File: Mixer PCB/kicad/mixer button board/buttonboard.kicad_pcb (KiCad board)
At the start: 2 copper layers, 161 x 57 mm, 58 parts, among them J1 Conn_01x02, J2 Conn_02x13_Odd_Even, sw1 cherry_sk6812, sw10 cherry_sk6812, sw11 cherry_sk6812, sw12 cherry_sk6812, sw13 cherry_sk6812, sw14 cherry_sk6812, sw15 cherry_sk6812, sw16 cherry_sk6812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

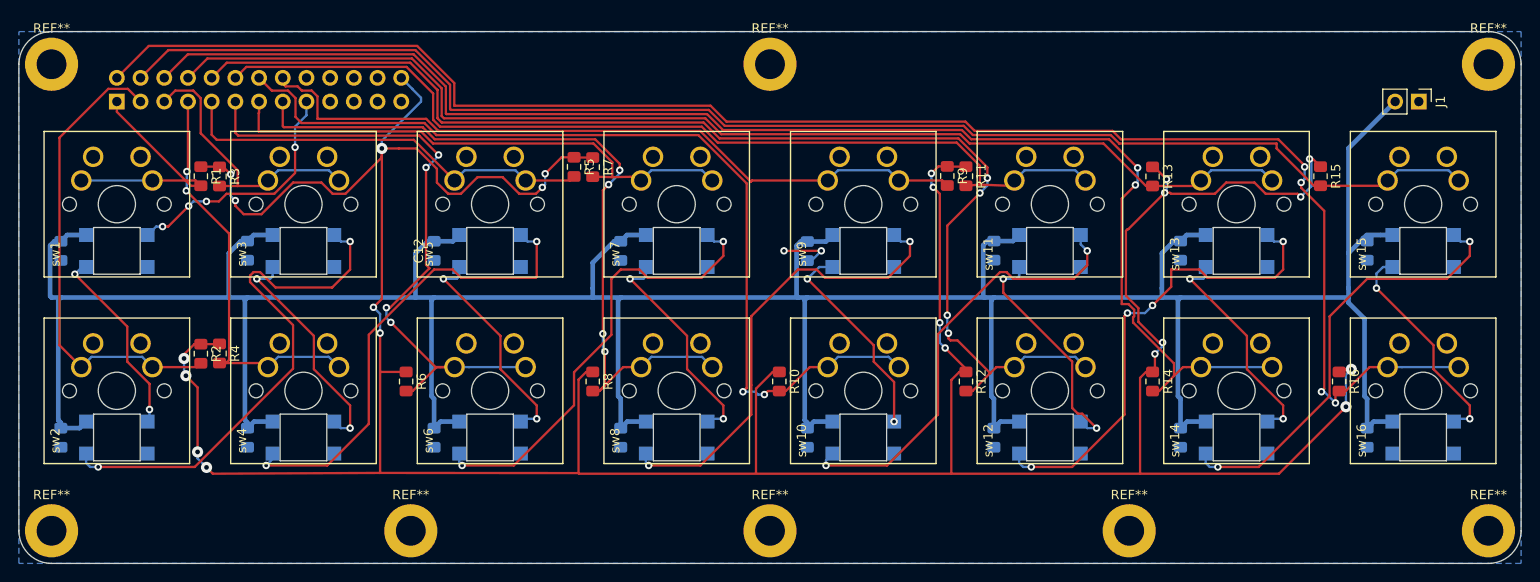
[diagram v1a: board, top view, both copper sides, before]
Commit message: Updated Button board to I2C
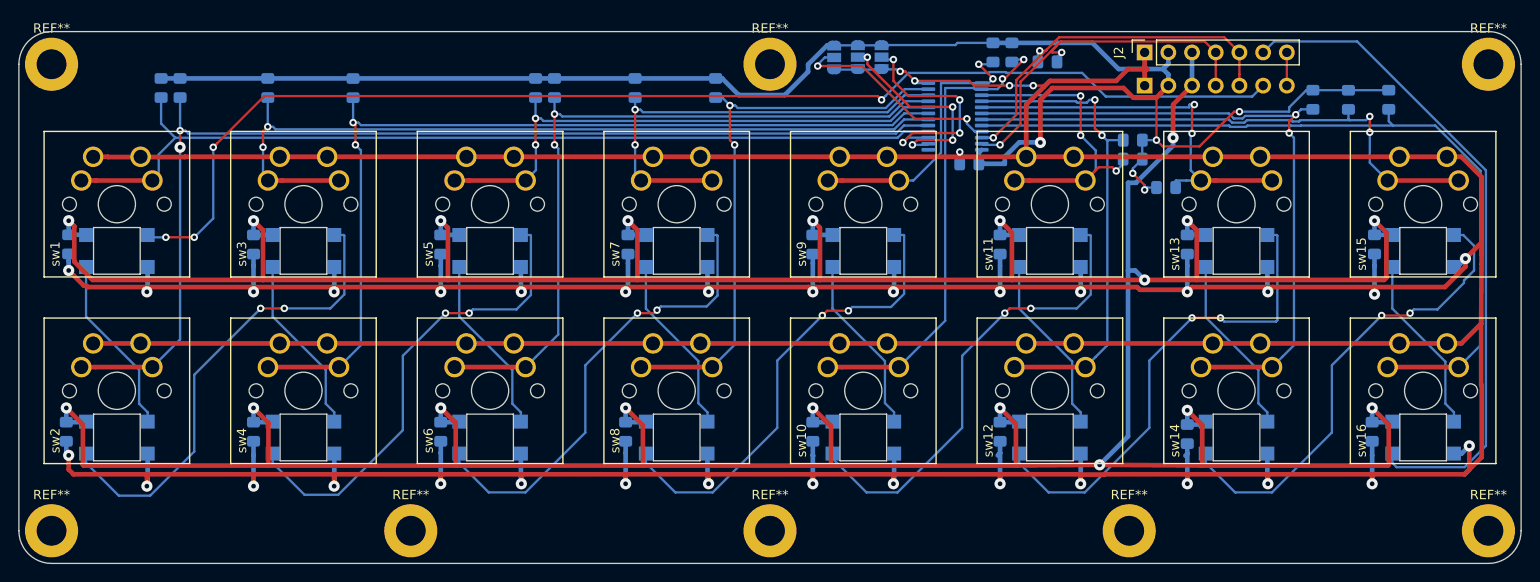
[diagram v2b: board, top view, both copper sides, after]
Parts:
- added C17: C, Capacitor_SMD:C_0805_2012Metric_Pad1.15x1.40mm_HandSolder, B.Cu at (181.4, 185.7)
- added JP1: SolderJumper_3_Open, Jumper:SolderJumper-3_P1.3mm_Open_RoundedPad1.0x1.5mm, B.Cu at (166.9, 174.3)
- added JP2: SolderJumper_3_Open, Jumper:SolderJumper-3_P1.3mm_Open_RoundedPad1.0x1.5mm, B.Cu at (169.4, 174.2)
- added JP3: SolderJumper_3_Open, Jumper:SolderJumper-3_P1.3mm_Open_RoundedPad1.0x1.5mm, B.Cu at (172.0, 174.2)
- added R17: 120, Resistor_SMD:R_0805_2012Metric_Pad1.15x1.40mm_HandSolder, B.Cu at (189.7, 174.8)
- added ic1: PCA9555, Package_SO:TSSOP-24_4.4x7.8mm_P0.65mm, B.Cu at (179.8, 180.6)
- J1: value Conn_01x02 -> Conn_01x07; footprint Connector_PinHeader_2.54mm:PinHeader_1x02_P2.54mm_Vertical -> Connector_PinSocket_2.54mm:PinSocket_1x07_P2.54mm_Vertical; moved to B.Cu
- J2: value Conn_02x13_Odd_Even -> Conn_01x07; footprint Connector_PinSocket_2.54mm:PinSocket_2x13_P2.54mm_Vertical -> Connector_PinSocket_2.54mm:PinSocket_1x07_P2.54mm_Vertical; moved to F.Cu
- R1, R10, R11, R12, R13, R14, R15, R16, R2, R3, R4, R5, R6, R7, R8, R9: moved to B.Cu
- moved J2 110.3 mm to (200.2, 173.7), turned to 90 degrees
- moved C10 100.7 mm to (204.7, 194.3)
- moved C7 99.4 mm to (104.6, 214.4)
- moved C4 81.9 mm to (144.8, 194.3)
- moved C8 60.8 mm to (224.8, 194.3)
- moved C13 60.6 mm to (164.6, 214.4)
- moved C2 59.3 mm to (124.7, 194.3)
- moved C9 45.6 mm to (164.6, 194.3)
- moved R10 43.2 mm to (185.9, 173.7)
- moved C5 40.7 mm to (204.7, 214.6)
- moved C16 40.7 mm to (184.7, 194.3)
- moved C6 39.5 mm to (144.5, 214.4)
- moved R6 35.2 mm to (136.9, 177.5)
- moved R14 34.7 mm to (218.2, 178.8)
- moved R8 34.1 mm to (154.2, 177.5)
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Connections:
- J1 pad 2: +5V -> +3V3
- J2 pad 1: Button1 -> GND
- J2 pad 2: Button16 -> +3V3
- J2 pad 3: Button2 -> +5V
- J2 pad 4: Button15 -> SDA
- J2 pad 5: Button3 -> SCL
- J2 pad 6: Button14 -> LEDOUT
- J2 pad 7: Button4 -> LEDOUT1
- sw1 pad 3: LED1 -> LEDIN
- sw10 pad 4: Net-(sw10-Pad4) -> GND
- sw16 pad 6: ledout -> LEDOUT
- sw2 pad 4: Net-(sw2-Pad4) -> GND
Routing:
- net GND: track 5.93 -> 971.5 mm, vias 2 -> 37
- net +3V3: track 377.3 -> 189.3 mm, vias 23 -> 5
- net LEDIN: track 0.00 -> 133.4 mm, vias 0 -> 4
- net +5V: track 377.9 -> 496.2 mm, vias 0 -> 19
- net Button15: track 151.5 -> 58.6 mm, vias 0 -> 2
- net Button16: track 178.3 -> 87.2 mm, vias 4 -> 0
- net Button13: track 125.6 -> 42.9 mm, vias 0 -> 2
- net Button14: track 151.8 -> 72.3 mm
- net Button12: track 131.2 -> 51.8 mm, vias 4 -> 2
- net Button1: track 26.4 -> 99.1 mm
- net LEDOUT: track 0.00 -> 71.8 mm
- net Button11: track 102.3 -> 34.1 mm, vias 0 -> 3
- net Button2: track 50.9 -> 118.4 mm, vias 0 -> 2
- net Button3: track 29.8 -> 88.3 mm, vias 0 -> 2
- net Button4: track 44.7 -> 100.1 mm
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- removed copper zone on B.Cu, net GND
